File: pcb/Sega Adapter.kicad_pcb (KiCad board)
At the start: 2 copper layers, 6 parts, among them J1 Sega, J2 Atari, J3 ICSP, SW1 C64, U1 PIC16F1847

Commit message: Finished schematic
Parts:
- removed SW1: C64, Button_Switch_THT:SW_E-Switch_EG1224_SPDT_Angled
- added JP1: Prog/C64, Connector_PinHeader_2.54mm:PinHeader_1x03_P2.54mm_Vertical, F.Cu at (139.7, 115.6)
- Atari: renamed from J2; footprint Connector_Dsub:DSUB-9_Male_Horizontal_P2.77x2.84mm_EdgePinOffset4.94mm_Housed_MountingHolesOffset7.48mm -> Connector_Dsub:DSUB-9_Female_Horizontal_P2.77x2.84mm_EdgePinOffset7.70mm_Housed_MountingHolesOffset9.12mm
- J3: footprint Connector_PinHeader_2.54mm:PinHeader_1x06_P2.54mm_Horizontal -> Connector_PinHeader_2.54mm:PinHeader_1x06_P2.54mm_Vertical
- SEGA: renamed from J1; footprint Connector_Dsub:DSUB-9_Female_Horizontal_P2.77x2.84mm_EdgePinOffset4.94mm_Housed_MountingHolesOffset7.48mm -> Connector_Dsub:DSUB-9_Male_Horizontal_P2.77x2.84mm_EdgePinOffset7.70mm_Housed_MountingHolesOffset9.12mm
- moved J3 30.2 mm to (133.3, 115.6)
- moved U1 23.9 mm to (139.7, 128.3), turned to 90 degrees
- moved Atari 22.6 mm to (141.0, 108.0)
- moved SEGA 17.8 mm to (141.0, 135.9)
- moved C1 14.2 mm to (152.5, 115.6)
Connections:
- net Net-(C1-Pad2) renamed +5V
- Atari pad 0: Net-(J2-Pad0) -> GND
- Atari pad 8: Net-(C1-Pad1) -> GND
- C1 pad 1: Net-(C1-Pad1) -> GND
- J3 pad 3: Net-(C1-Pad1) -> GND
- SEGA pad 0: Net-(J1-Pad0) -> GND
- SEGA pad 8: Net-(C1-Pad1) -> GND
- U1 pad 5: Net-(C1-Pad1) -> GND
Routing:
- net +5V: track 0.00 -> 79.8 mm
- net Net-(J1-Pad6): track 0.00 -> 41.7 mm
- net Net-(J1-Pad7): track 0.00 -> 38.4 mm
- net Net-(J2-Pad9): track 0.00 -> 28.8 mm, vias 0 -> 2
- net Net-(J2-Pad5): track 0.00 -> 28.4 mm, vias 0 -> 1
- net Net-(J2-Pad6): track 0.00 -> 27.4 mm
- net Net-(J1-Pad9): track 0.00 -> 21.7 mm, vias 0 -> 2
- net Net-(JP1-Pad2): track 0.00 -> 14.8 mm
- net Net-(J1-Pad1): track 0.00 -> 14.6 mm
- net Net-(J1-Pad2): track 0.00 -> 14.4 mm
- net Net-(J2-Pad1): track 0.00 -> 14.3 mm
- net Net-(J2-Pad2): track 0.00 -> 14.3 mm
- net Net-(J1-Pad3): track 0.00 -> 14.1 mm
- net Net-(J1-Pad4): track 0.00 -> 13.9 mm
- net Net-(J2-Pad4): track 0.00 -> 13.5 mm
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- added copper zone on B.Cu, net GND
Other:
- board outline added: 36.2 x 45.7 mm
- net class Default: clearance 0.2 -> 0.1524; trace_width 0.25 -> 0.1524; via_dia 0.8 -> 0.6858; via_drill 0.4 -> 0.3302
- rule pad_to_mask_clearance: 0 -> 0.0508
- rule trace_clearance: 0.2 -> 0.1524
- rule trace_min: 0.2 -> 0.1524
- rule via_min_drill: 0.3 -> 0.254
- rule via_min_size: 0.4 -> 0.508
- board text added: "CLK"
- board text added: "DAT"
- board text added: "NC"
- board text added: "Vdd"
- board text added: "Vpp"
- board text added: "Vss"

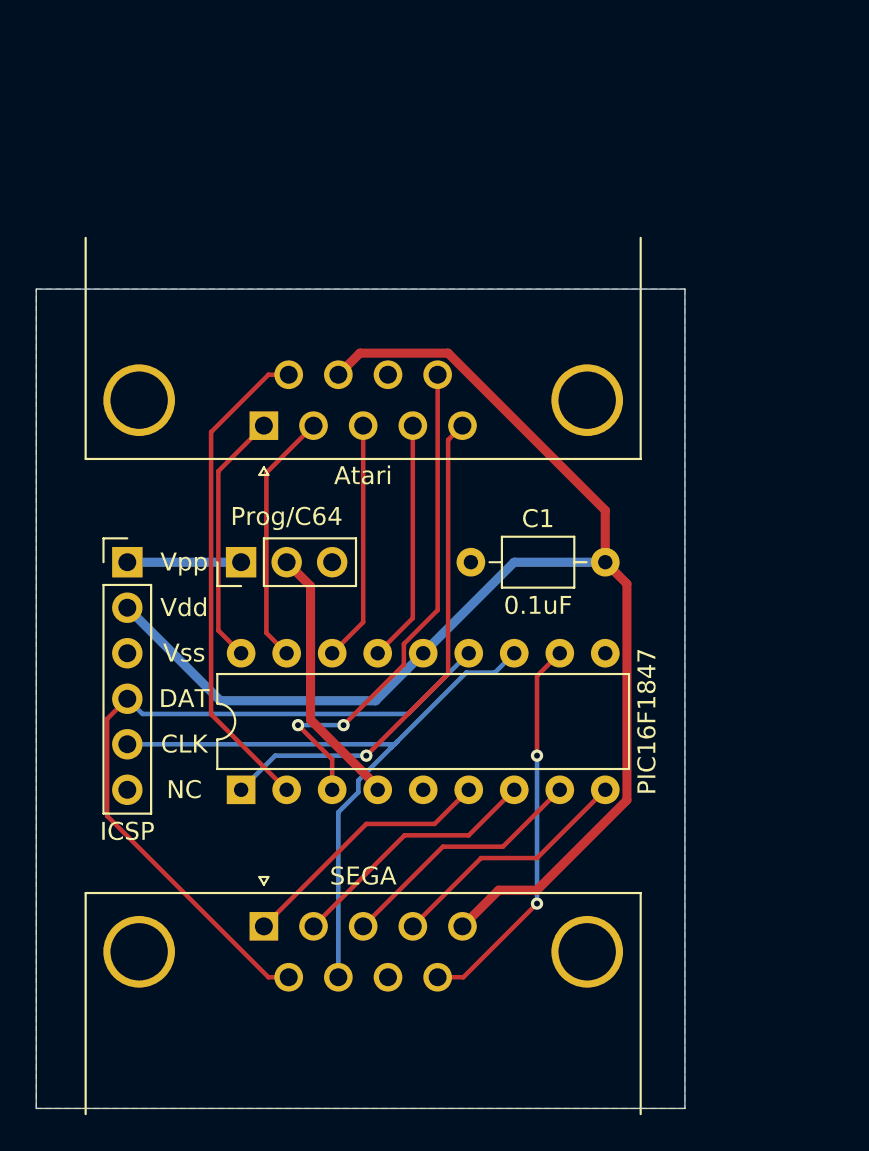
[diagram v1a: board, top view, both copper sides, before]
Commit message: More compact PCB
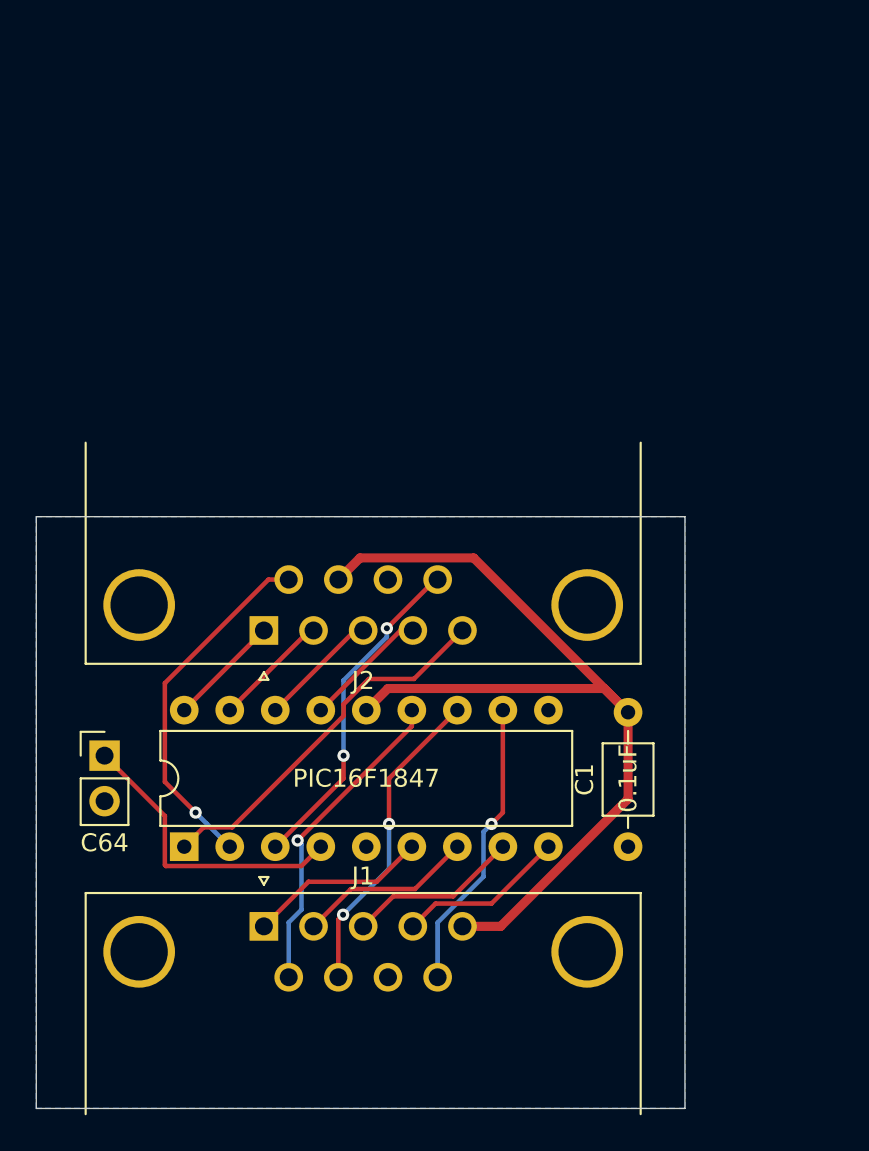
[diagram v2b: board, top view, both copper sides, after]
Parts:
- removed J3: ICSP, Connector_PinHeader_2.54mm:PinHeader_1x06_P2.54mm_Vertical
- JP1: value Prog/C64 -> C64; footprint Connector_PinHeader_2.54mm:PinHeader_1x03_P2.54mm_Vertical -> Connector_PinHeader_2.54mm:PinHeader_1x02_P2.54mm_Vertical
- moved C1 18.1 mm to (161.3, 131.4), turned to 90 degrees
- moved JP1 13.2 mm to (132.1, 126.4), turned to 0 degrees
- moved J2 11.4 mm to (141.0, 119.4)
- moved U1 4.49 mm to (136.5, 131.4)
- renumbered SEGA to J1, Atari to J2
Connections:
- JP1 pad 1: Net-(J3-Pad1) -> Net-(JP1-Pad1)
- JP1 pad 2: Net-(JP1-Pad2) -> GND
- U1 pad 4: Net-(JP1-Pad2) -> Net-(JP1-Pad1)
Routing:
- net +5V: track 79.8 -> 52.9 mm
- net Net-(J1-Pad6): track 41.7 -> 17.9 mm, vias 0 -> 1
- net Net-(J1-Pad7): track 38.4 -> 17.7 mm, vias 0 -> 2
- net Net-(JP1-Pad1): track 0.00 -> 16.7 mm
- net Net-(JP1-Pad2): track 14.8 -> 0.00 mm
- net Net-(J2-Pad9): track 28.8 -> 18.7 mm
- net Net-(J2-Pad1): track 14.3 -> 6.29 mm
- net Net-(J2-Pad2): track 14.3 -> 6.52 mm
- net Net-(J2-Pad5): track 28.4 -> 20.9 mm, vias 1 -> 0
- net Net-(J2-Pad6): track 27.4 -> 19.9 mm, vias 0 -> 1
- net Net-(J2-Pad3): track 13.4 -> 6.75 mm
- net Net-(J2-Pad4): track 13.5 -> 6.98 mm
- net Net-(J3-Pad1): track 6.35 -> 0.00 mm
- net Net-(J1-Pad9): track 21.7 -> 16.4 mm, vias 2 -> 1
- net Net-(J1-Pad4): track 13.9 -> 9.41 mm
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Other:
- board size 36.2 x 45.7 mm -> 36.2 x 33 mm
- board text removed: "CLK"
- board text removed: "DAT"
- board text removed: "NC"
- board text removed: "Vdd"
- board text removed: "Vpp"
- board text removed: "Vss"
